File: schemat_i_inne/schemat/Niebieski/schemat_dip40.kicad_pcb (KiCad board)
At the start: 2 copper layers, 208.3 x 76.2 mm, 18 parts, among them J1 Conn_01x06_Female, SW1 SW_DIP_x01, SW2 Left, SW3 Up, SW4 Down, SW5 Right, SW6 Jump, SW7 Punch, U1 ATmega32A-AU, U2 L7805, U3 WG12864B-STBL, U4 SD_card_reader, Y1 16Mhz

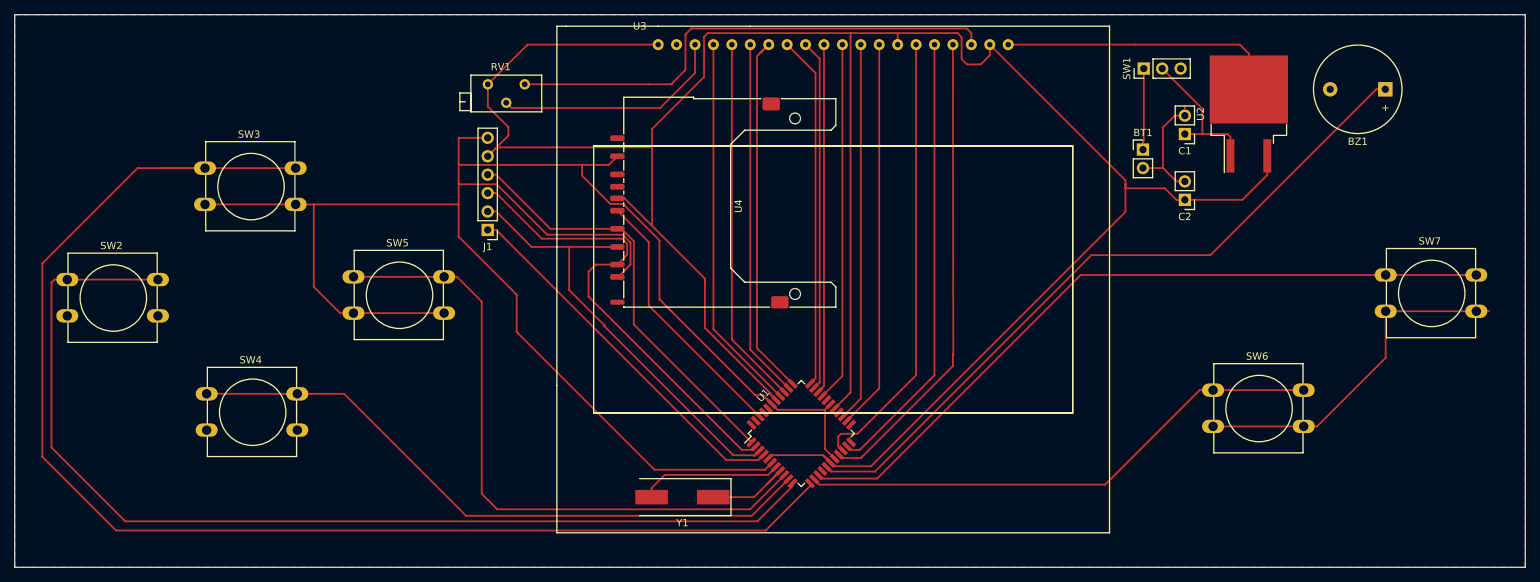
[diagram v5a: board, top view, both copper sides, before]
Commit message: Kolejne zmiany w szchemacie i plytce
->Dodano gniazdo ethernetowe i adapter zamiast zlacza 6pin
 aby byla mozliwa komunikacja miedzy konsolami
->zmieniono rozmieszczenie przyciskow
->drobne poprawki sciezek
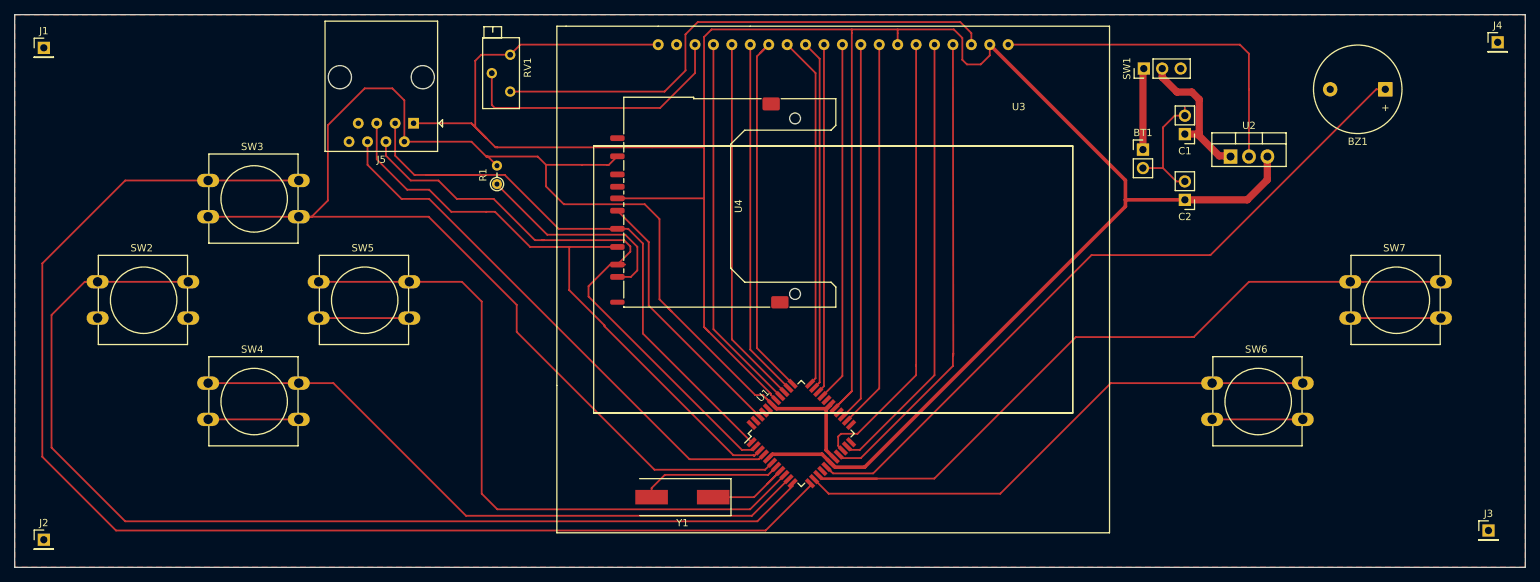
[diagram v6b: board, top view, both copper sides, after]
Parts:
- added J2: Hole2, Connector_PinHeader_2.54mm:PinHeader_1x01_P2.54mm_Vertical, F.Cu at (23.1, 100.3)
- added J3: Hole3, Connector_PinHeader_2.54mm:PinHeader_1x01_P2.54mm_Vertical, F.Cu at (222.2, 99.1)
- added J4: Hole4, Connector_PinHeader_2.54mm:PinHeader_1x01_P2.54mm_Vertical, F.Cu at (223.5, 31.8)
- added J5: RJ45, Connector_RJ:RJ45_Amphenol_54602-x08_Horizontal, F.Cu at (74.0, 42.9)
- added R1: 0R, Resistor_THT:R_Axial_DIN0204_L3.6mm_D1.6mm_P2.54mm_Vertical, F.Cu at (85.5, 51.3)
- J1: value Conn_01x06_Female -> Hole1; footprint Connector_PinHeader_2.54mm:PinHeader_1x06_P2.54mm_Vertical -> Connector_PinHeader_2.54mm:PinHeader_1x01_P2.54mm_Vertical
- U2: footprint Package_TO_SOT_SMD:TO-263-2 -> Package_TO_SOT_THT:TO-220-3_Vertical
- moved J1 66.1 mm to (23.1, 32.5), turned to 0 degrees
- moved U2 6.39 mm to (186.7, 47.5), turned to 0 degrees
- moved SW7 4.97 mm to (203.2, 64.8)
- moved SW5 4.85 mm to (61.0, 64.8)
- moved SW2 4.19 mm to (30.5, 64.8)
- moved RV1 2.23 mm to (87.4, 38.5), turned to 270 degrees
- moved SW3 1.76 mm to (45.7, 50.8)
- moved SW4 1.49 mm to (45.7, 78.7)
- moved SW6 0.97 mm to (184.2, 78.7)
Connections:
- U1 pad 1: Net-(J1-Pad4) -> Net-(J5-Pad3)
- U1 pad 2: Net-(J1-Pad3) -> Net-(J5-Pad4)
- U1 pad 3: Net-(J1-Pad2) -> Net-(J5-Pad5)
- U1 pad 4: Net-(J1-Pad1) -> Net-(J5-Pad6)
- U4 pad 5: Net-(J1-Pad4) -> Net-(J5-Pad3)
- U4 pad 6: Net-(J1-Pad2) -> Net-(J5-Pad5)
- U4 pad 7: Net-(J1-Pad3) -> Net-(J5-Pad4)
- U4 pad 8: GND -> Net-(R1-Pad1)
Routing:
- net Net-(J5-Pad5): track 0.00 -> 85.2 mm
- net Net-(J5-Pad3): track 0.00 -> 84.9 mm
- net Net-(J5-Pad4): track 0.00 -> 84.1 mm
- net Net-(J5-Pad6): track 0.00 -> 74.9 mm
- net Net-(J1-Pad3): track 65.4 -> 0.00 mm
- net Net-(J1-Pad2): track 62.0 -> 0.00 mm
- net Net-(J1-Pad4): track 58.4 -> 0.00 mm
- net Net-(J1-Pad1): track 51.5 -> 0.00 mm
- net Net-(R1-Pad1): track 0.00 -> 29.4 mm
- net VCC: track 350.2 -> 378.8 mm
- net GND: track 367.1 -> 349.2 mm
- net Net-(SW3-Pad1): track 186.1 -> 179.7 mm
- net Net-(RV1-Pad2): track 32.2 -> 38.5 mm
- net Net-(SW5-Pad1): track 90.2 -> 94.7 mm
- net Net-(RV1-Pad1): track 69.6 -> 72.7 mm
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
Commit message: Upraszczanie polaczen i poprawianie plytki
Gotowe polaczenia do ekranu
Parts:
- removed J5: RJ45, Connector_RJ:RJ45_Amphenol_54602-x08_Horizontal
- removed RV1: R_POT, Potentiometer_THT:Potentiometer_Bourns_3296Z_Horizontal
- removed SW4: Down, Button_Switch_THT:SW_PUSH-12mm
- removed SW5: Right, Button_Switch_THT:SW_PUSH-12mm
- removed SW6: Jump, Button_Switch_THT:SW_PUSH-12mm
- removed SW7: Punch, Button_Switch_THT:SW_PUSH-12mm
- removed U4: SD_card_reader, Connector_Card:SD_Kyocera_145638009511859+
- removed Y1: 16Mhz, Crystal:Crystal_SMD_HC49-SD
- BT1, BZ1, C1, C2, R1, SW1, SW2, SW3, U2, U3: moved to B.Cu
- moved BZ1 60.8 mm to (195.6, 97.8), turned to 0 degrees
- moved U3 51.4 mm to (159.1, 72.4), turned to 180 degrees
- moved SW3 46.7 mm to (78.7, 83.8), turned to 180 degrees
- moved SW2 45.8 mm to (63.5, 96.5), turned to 180 degrees
- moved U2 37.4 mm to (213.4, 73.7)
- moved SW1 37.3 mm to (201.9, 61.0)
- moved U1 33.3 mm to (149.1, 111.1), turned to 135 degrees
- moved C2 33.3 mm to (202.0, 78.9)
- moved BT1 33.3 mm to (196.2, 71.9)
- moved C1 33.3 mm to (202.0, 69.8)
- moved J2 33.2 mm to (44.5, 125.7)
- moved J1 32.6 mm to (44.5, 57.1)
- moved J3 27.9 mm to (233.7, 124.5)
- moved J4 27.4 mm to (233.7, 57.1)
- moved R1 13.5 mm to (85.1, 64.8), turned to 270 degrees
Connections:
- SW1 pad 1: Net-(BT1-Pad1) -> Net-(C1-Pad1)
- SW1 pad 2: Net-(C1-Pad1) -> Net-(BT1-Pad1)
- U1 pad 11: Net-(SW2-Pad1) -> Net-(U1-Pad11)
- U1 pad 12: Net-(SW3-Pad1) -> Net-(U1-Pad12)
- U1 pad 13: Net-(SW6-Pad1) -> Net-(U1-Pad13)
- U1 pad 14: Net-(SW7-Pad1) -> Net-(U1-Pad14)
- U1 pad 16: Net-(BZ1-Pad1) -> Net-(U1-Pad16)
- U1 pad 31: Net-(U1-Pad31) -> Net-(SW7-Pad1)
- U1 pad 32: Net-(U1-Pad32) -> Net-(SW6-Pad1)
- U1 pad 33: Net-(U1-Pad33) -> Net-(SW5-Pad1)
- U1 pad 34: Net-(U1-Pad34) -> Net-(SW2-Pad1)
- U1 pad 35: Net-(U1-Pad35) -> Net-(SW4-Pad1)
- U1 pad 36: Net-(U1-Pad36) -> Net-(SW3-Pad1)
- U1 pad 37: Net-(U1-Pad37) -> Net-(BZ1-Pad1)
- U3 pad 1: VCC -> Net-(U1-Pad12)
- U3 pad 10: Net-(U1-Pad31) -> Net-(U1-Pad20)
- U3 pad 11: Net-(U1-Pad30) -> Net-(U1-Pad21)
- U3 pad 12: Net-(U1-Pad25) -> Net-(U1-Pad22)
- U3 pad 13: Net-(U1-Pad24) -> Net-(U1-Pad23)
- U3 pad 14: VCC -> Net-(U1-Pad24)
- U3 pad 15: Net-(U1-Pad20) -> Net-(U1-Pad25)
- U3 pad 16: Net-(U1-Pad21) -> Net-(U1-Pad26)
- U3 pad 17: Net-(U1-Pad19) -> VCC
- U3 pad 2: GND -> Net-(U1-Pad13)
- U3 pad 3: Net-(RV1-Pad2) -> GND
- U3 pad 4: Net-(U1-Pad37) -> VCC
- U3 pad 5: Net-(U1-Pad36) -> Net-(RV1-Pad2)
- U3 pad 6: Net-(U1-Pad35) -> Net-(U1-Pad15)
- U3 pad 7: Net-(U1-Pad34) -> Net-(U1-Pad16)
- U3 pad 8: Net-(U1-Pad33) -> Net-(U1-Pad14)
- U3 pad 9: Net-(U1-Pad32) -> Net-(U1-Pad19)
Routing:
- net VCC: track 378.8 -> 233.3 mm
- net Net-(SW7-Pad1): track 105.2 -> 0.00 mm
- net Net-(U1-Pad9): track 94.7 -> 0.00 mm
- net Net-(U1-Pad10): track 89.7 -> 0.00 mm
- net Net-(J5-Pad5): track 85.2 -> 0.00 mm
- net Net-(J5-Pad3): track 84.9 -> 0.00 mm
- net Net-(J5-Pad4): track 84.1 -> 0.00 mm
- net Net-(J5-Pad6): track 74.9 -> 0.00 mm
- net Net-(SW6-Pad1): track 74.5 -> 0.00 mm
- net Net-(RV1-Pad1): track 72.7 -> 0.00 mm
- net Net-(U1-Pad14): track 0.00 -> 55.9 mm
- net Net-(U1-Pad12): track 0.00 -> 53.9 mm
- net Net-(U1-Pad13): track 0.00 -> 52.5 mm
- net Net-(U1-Pad37): track 52.3 -> 0.00 mm
- net Net-(U1-Pad26): track 0.00 -> 51.7 mm
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- removed copper zone on F.Cu, net GND
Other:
- board size 208.3 x 76.2 mm -> 260.4 x 151.1 mm

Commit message: Wiele elementow dodanych
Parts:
- added RV1: R_POT, Potentiometer_THT:Potentiometer_Bourns_3296Z_Horizontal, B.Cu at (102.4, 62.5)
- added SW4: Down, Button_Switch_THT:SW_PUSH-12mm, B.Cu at (66.0, 111.8)
- added SW5: Right, Button_Switch_THT:SW_PUSH-12mm, B.Cu at (81.3, 101.6)
- added SW6: Jump, Button_Switch_THT:SW_PUSH-12mm, B.Cu at (194.3, 111.8)
- added SW7: Punch, Button_Switch_THT:SW_PUSH-12mm, B.Cu at (209.6, 101.6)
- added U4: SD_card_reader, Connector_Card:SD_Kyocera_145638009511859+, F.Cu at (157.5, 116.8)
- added Y1: 16Mhz, Crystal:Crystal_SMD_HC49-SD, F.Cu at (137.2, 115.6)
- R1: footprint Resistor_THT:R_Axial_DIN0204_L3.6mm_D1.6mm_P2.54mm_Vertical -> Resistor_THT:R_Axial_DIN0204_L3.6mm_D1.6mm_P7.62mm_Horizontal; moved to F.Cu
- moved BZ1 98.8 mm to (100.1, 122.9), turned to 180 degrees
- moved U1 28.5 mm to (120.7, 110.5)
- moved U2 19.1 mm to (199.3, 60.7)
- moved C2 13.0 mm to (204.8, 66.1), turned to 90 degrees
- moved R1 12.7 mm to (92.7, 74.9), turned to 90 degrees
- moved C1 11.8 mm to (194.7, 60.6)
- moved SW1 11.0 mm to (191.0, 60.1)
- moved BT1 9.54 mm to (188.3, 66.6)
- moved SW3 2.54 mm to (78.7, 86.4)
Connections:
- U3 pad 3: GND -> Net-(R1-Pad1)
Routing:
- net Net-(SW6-Pad1): track 0.00 -> 262.1 mm
- net GND: track 352.9 -> 607.3 mm
- net Net-(SW7-Pad1): track 0.00 -> 244.2 mm
- net VCC: track 233.3 -> 391.9 mm
- net Net-(SW5-Pad1): track 0.00 -> 94.0 mm
- net Net-(R1-Pad1): track 0.00 -> 78.9 mm
- net Net-(SW3-Pad1): track 141.1 -> 62.7 mm
- net Net-(RV1-Pad2): track 0.00 -> 73.9 mm
- net Net-(SW4-Pad1): track 0.00 -> 49.2 mm
- net Net-(BZ1-Pad1): track 65.2 -> 19.4 mm
- net Net-(U1-Pad44): track 0.00 -> 44.5 mm
- net Net-(J5-Pad4): track 0.00 -> 35.3 mm
- net Net-(J5-Pad5): track 0.00 -> 33.5 mm
- net Net-(J5-Pad3): track 0.00 -> 29.5 mm
- net Net-(SW2-Pad1): track 98.4 -> 69.7 mm
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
